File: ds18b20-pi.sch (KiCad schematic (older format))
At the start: 29 parts, among them J1 Conn_01x03_Female, J2 Conn_01x03_Female, J3 Conn_01x02_Female, J4 Conn_01x02_Female, J5 Conn_01x02_Female, J6 Conn_01x02_Female, J7 Conn_01x02_Female, J8 Conn_01x02_Female, J9 Conn_01x02_Female, K1 TIANBO-HJR-4102-L, K2 TIANBO-HJR-4102-L, K3 TIANBO-HJR-4102-L, K4 TIANBO-HJR-4102-L, K5 TIANBO-HJR-4102-L, K6 TIANBO-HJR-4102-L, P1 CONN_13X2, Q1 2N7000, Q2 2N7000, Q3 2N7000, Q4 2N7000, Q5 2N7000, Q6 2N7000

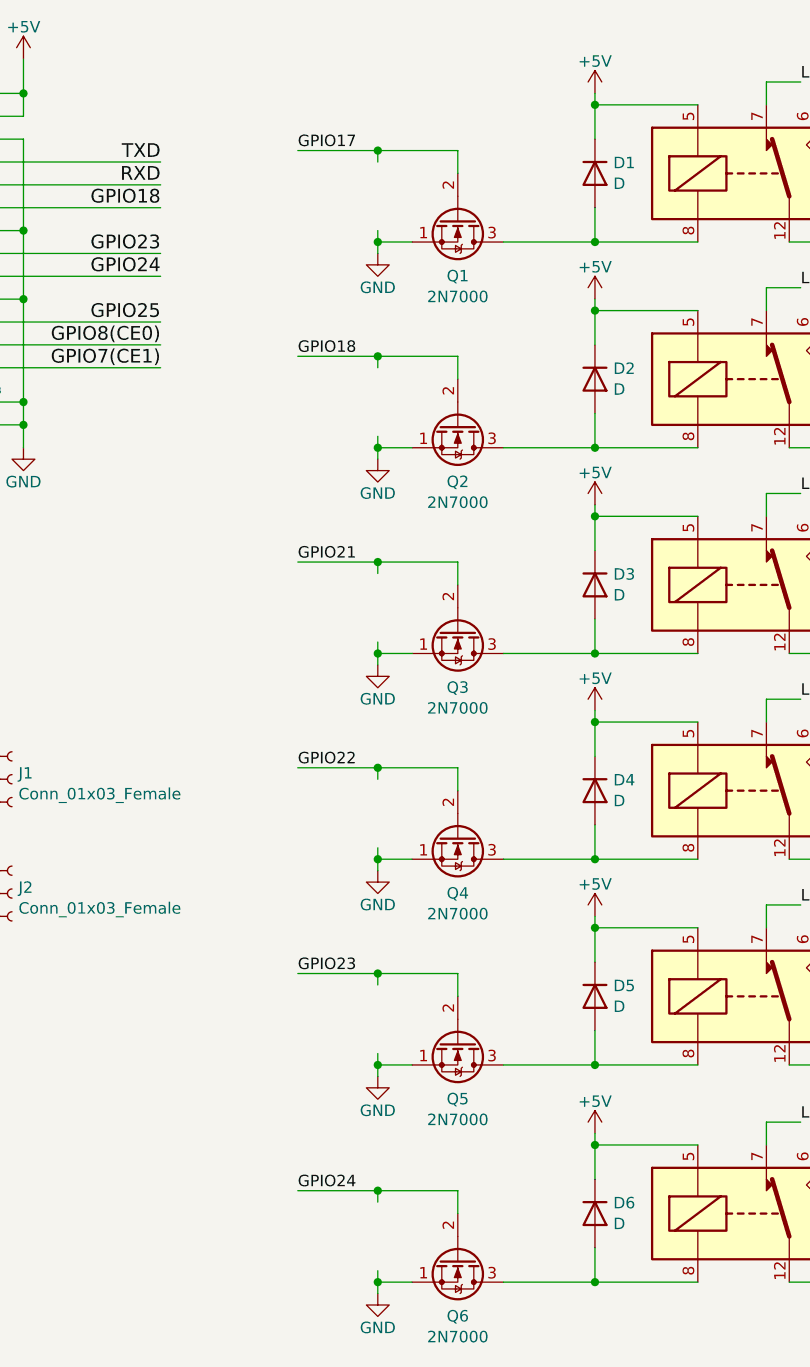
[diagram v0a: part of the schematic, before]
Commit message: Indicator led for each relay
There are leds that already have a series resistor included to limit the
current. Those leds are necessary for this board, because there is not
enough space for addition resistors.
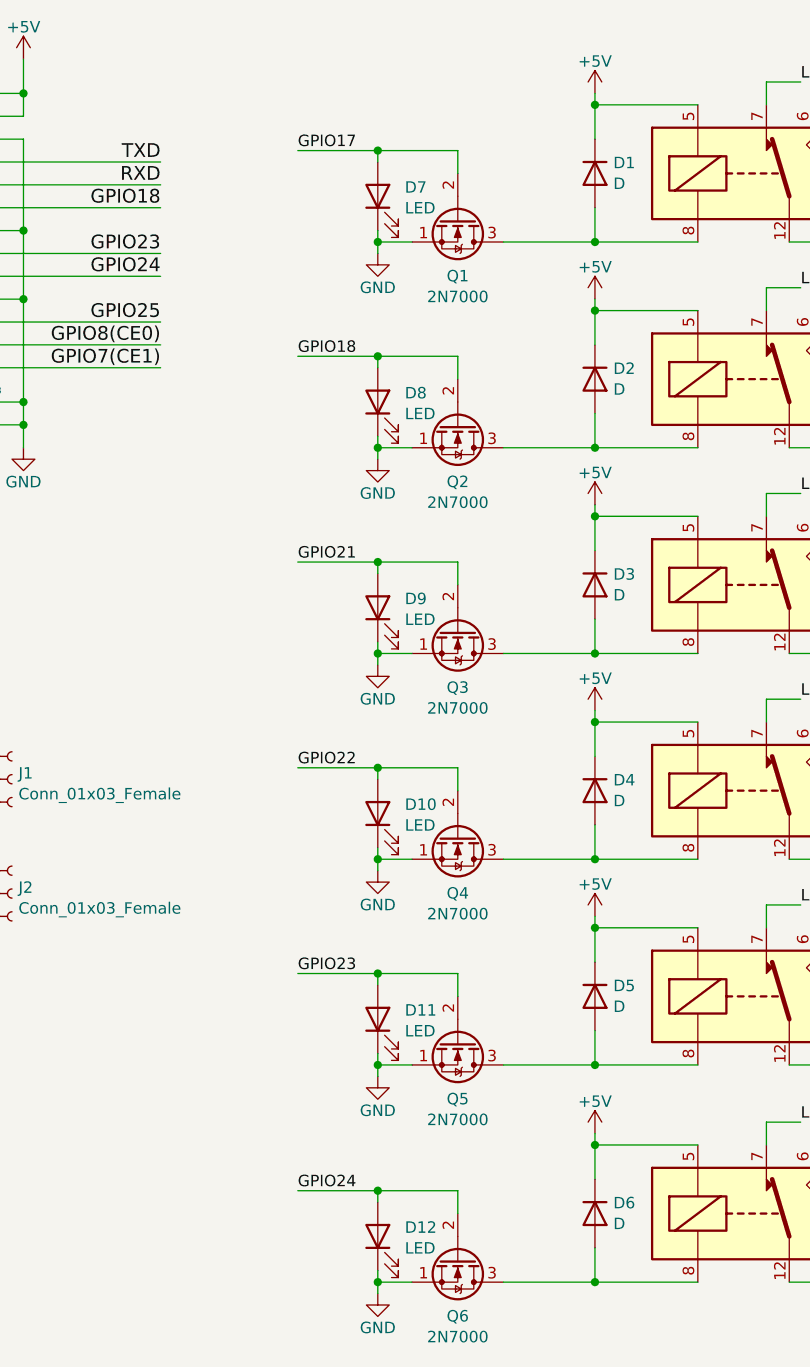
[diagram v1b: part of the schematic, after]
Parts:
- added D10, D11, D12, D7, D8, D9: LED, LED_THT:LED_D3.0mm, symbol Device:LED
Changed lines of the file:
@@
 Sheet 1 1
 Title "ds18b20 raspberry pi 1"
-Date "2020-05-30"
-Rev "B"
+Date "2020-06-03"
+Rev "C"
 Comp ""
 Comment1 "ts"
@@
 Text Label 6850 1250 0    50   ~ 0
 N
+$Comp
+L Device:LED D7
+U 1 1 5ED75065
+P 3850 1400
+F 0 "D7" V 3889 1282 50  0000 R CNN
+F 1 "LED" V 3798 1282 50  0000 R CNN
+F 2 "LED_THT:LED_D3.0mm" H 3850 1400 50  0001 C CNN
+F 3 "~" H 3850 1400 50  0001 C CNN
+	1    3850 1400
+	0    -1   -1   0
+$EndComp
+$Comp
+L Device:LED D8
+U 1 1 5ED8074D
+P 3850 2300
+F 0 "D8" V 3889 2182 50  0000 R CNN
+F 1 "LED" V 3798 2182 50  0000 R CNN
+F 2 "LED_THT:LED_D3.0mm" H 3850 2300 50  0001 C CNN
+F 3 "~" H 3850 2300 50  0001 C CNN
+	1    3850 2300
+	0    -1   -1   0
+$EndComp
+$Comp
+L Device:LED D9
+U 1 1 5ED80D78
+P 3850 3200
+F 0 "D9" V 3889 3082 50  0000 R CNN
+F 1 "LED" V 3798 3082 50  0000 R CNN
+F 2 "LED_THT:LED_D3.0mm" H 3850 3200 50  0001 C CNN
+F 3 "~" H 3850 3200 50  0001 C CNN
+	1    3850 3200
+	0    -1   -1   0
+$EndComp
+$Comp
+L Device:LED D10
+U 1 1 5ED83563
+P 3850 4100
+F 0 "D10" V 3889 3982 50  0000 R CNN
+F 1 "LED" V 3798 3982 50  0000 R CNN
+F 2 "LED_THT:LED_D3.0mm" H 3850 4100 50  0001 C CNN
+F 3 "~" H 3850 4100 50  0001 C CNN
+	1    3850 4100
+	0    -1   -1   0
+$EndComp
+$Comp
+L Device:LED D11
+U 1 1 5ED83AFA
+P 3850 5000
+F 0 "D11" V 3889 4882 50  0000 R CNN
+F 1 "LED" V 3798 4882 50  0000 R CNN
+F 2 "LED_THT:LED_D3.0mm" H 3850 5000 50  0001 C CNN
+F 3 "~" H 3850 5000 50  0001 C CNN
+	1    3850 5000
+	0    -1   -1   0
+$EndComp
+$Comp
+L Device:LED D12
+U 1 1 5ED8592F
+P 3850 5950
+F 0 "D12" V 3889 5832 50  0000 R CNN
+F 1 "LED" V 3798 5832 50  0000 R CNN
+F 2 "LED_THT:LED_D3.0mm" H 3850 5950 50  0001 C CNN
+F 3 "~" H 3850 5950 50  0001 C CNN
+	1    3850 5950
+	0    -1   -1   0
+$EndComp
 $EndSCHEMATC

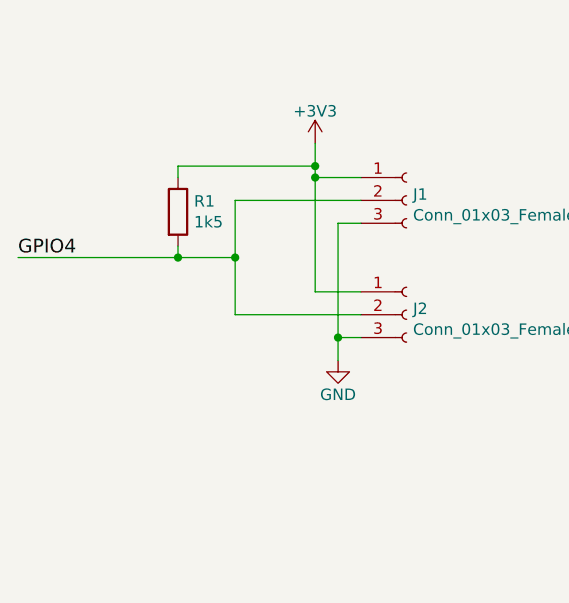
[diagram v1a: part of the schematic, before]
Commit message: tvs diode
The sensors are connected through long wires, which make it very likely
for radiation to couple into them and disturb the communication.
Therefore a tvs diode was added. Unfortunately for a breakdown voltage
of 3,3V there are only smd packages available.
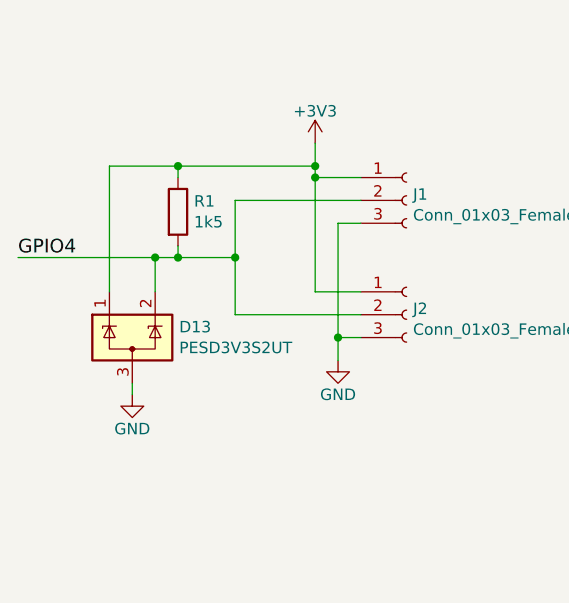
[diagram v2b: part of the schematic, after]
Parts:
- added D13: PESD3V3S2UT, Package_TO_SOT_SMD:SOT-23, symbol Power_Protection:SP0502BAHT
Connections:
- net +3V3: now also D13.1 (K)
- net GND: now also D13.3 (A)
- net GPIO4: now also D13.2 (K)
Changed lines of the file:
@@
 Title "ds18b20 raspberry pi 1"
 Date "2020-06-03"
-Rev "C"
+Rev "D"
 Comp ""
 Comment1 "ts"
 Comment2 ""
 Comment3 ""
-Comment4 "heating controll"
+Comment4 "heating control"
 $EndDescr
 $Comp
@@
 GPIO4
 Wire Wire Line
-	550  4200 1250 4200
+	550  4200 1150 4200
 Connection ~ 1500 4200
 Wire Wire Line
@@
 	0    -1   -1   0
 $EndComp
+$Comp
+L Power_Protection:SP0502BAHT D13
+U 1 1 5EE5A541
+P 1050 4550
+F 0 "D13" H 1255 4596 50  0000 L CNN
+F 1 "PESD3V3S2UT" H 1255 4505 50  0000 L CNN
+F 2 "Package_TO_SOT_SMD:SOT-23" H 1275 4500 50  0001 L CNN
+F 3 "http://www.littelfuse.com/~/media/files/littelfuse/technical%20resources/documents/data%20sheets/sp05xxba.pdf" H 1175 4675 50  0001 C CNN
+	1    1050 4550
+	1    0    0    -1
+$EndComp
+Wire Wire Line
+	950  4350 950  3800
+Wire Wire Line
+	950  3800 1250 3800
+Connection ~ 1250 3800
+Wire Wire Line
+	1150 4350 1150 4200
+Connection ~ 1150 4200
+Wire Wire Line
+	1150 4200 1250 4200
+$Comp
+L power:GND #PWR06
+U 1 1 5EE69ECE
+P 1050 4800
+F 0 "#PWR06" H 1050 4550 50  0001 C CNN
+F 1 "GND" H 1050 4650 50  0000 C CNN
+F 2 "" H 1050 4800 50  0000 C CNN
+F 3 "" H 1050 4800 50  0000 C CNN
+	1    1050 4800
+	1    0    0    -1
+$EndComp
+Wire Wire Line
+	1050 4750 1050 4800
 $EndSCHEMATC
